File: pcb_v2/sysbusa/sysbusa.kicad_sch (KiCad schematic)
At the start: 62 parts, among them J1 bus ula 2, J10 bus rf16 3, J11 bus clu 2, J12 bus clu 3, J19 9V 1A, J2 bus ula 1, J20 VOLTMETER, J21 AMPMETER, J22 bus ioc 2, J23 bus ioc 1, J24 bus ioc 3, J26 bus clock, J3 bus rf16 1, J4 bus rf16 2, J5 bus mem 1, J6 bus mem 2, J7 bus clu 1, Q1 BC548, Q2 BC548, SW1 RESET, U1 MC14495P, U10 MC14495P, U11 ADDR N1, U12 DATA N0, U13 MC14495P, U14 RDADDR_LOW, U17 RDADDR_HIGH, U2 ADDR N3, U21 MC14495P, U22 WRADDR_HIGH, U23 WRADDR_LOW, U3 MC14495P, U31 MC14495P, U34 LM7805, U4 ADDR N2, U6 MC14495P, U7 DATA N1, U8 MC14495P, U9 ADDR N0

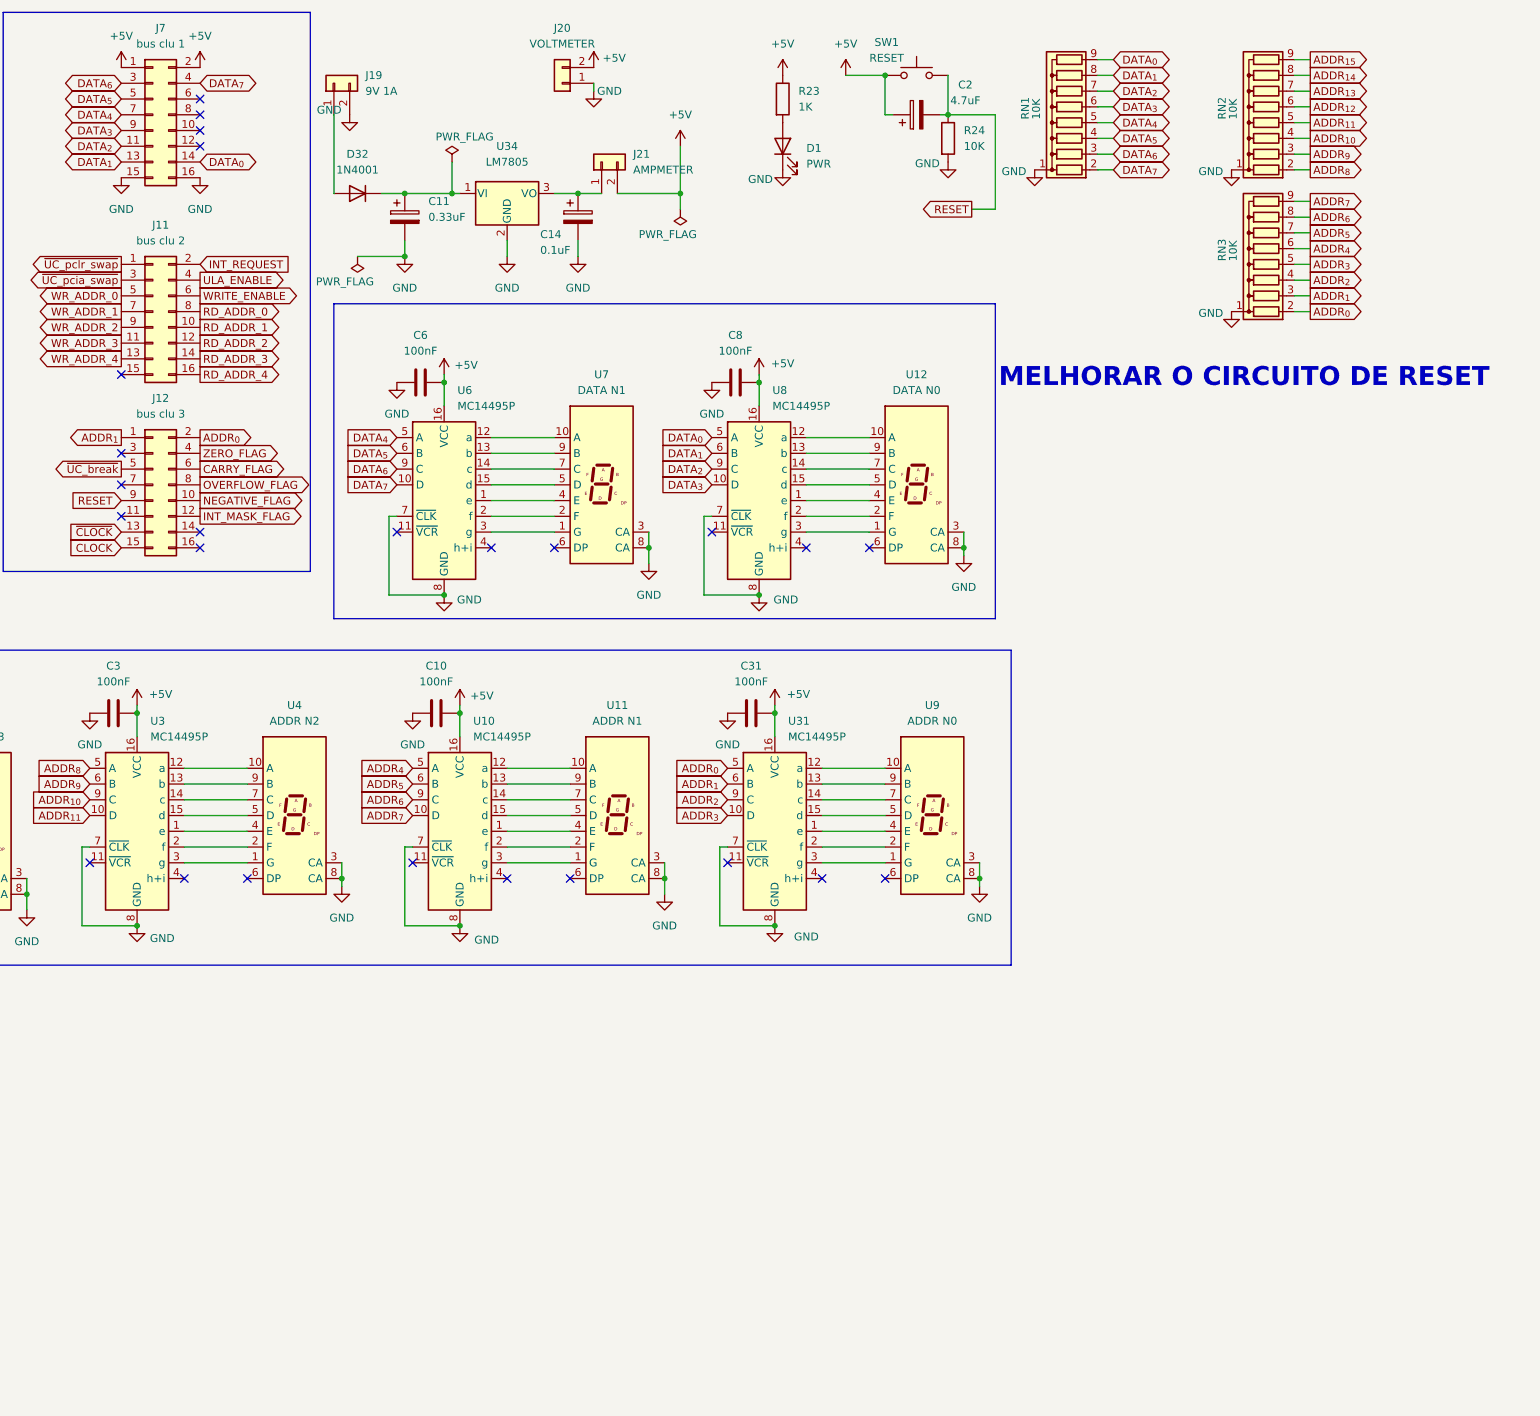
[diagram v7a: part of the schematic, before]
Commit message: melhoria no reset, para que seja acionado automaticamente ao ligar
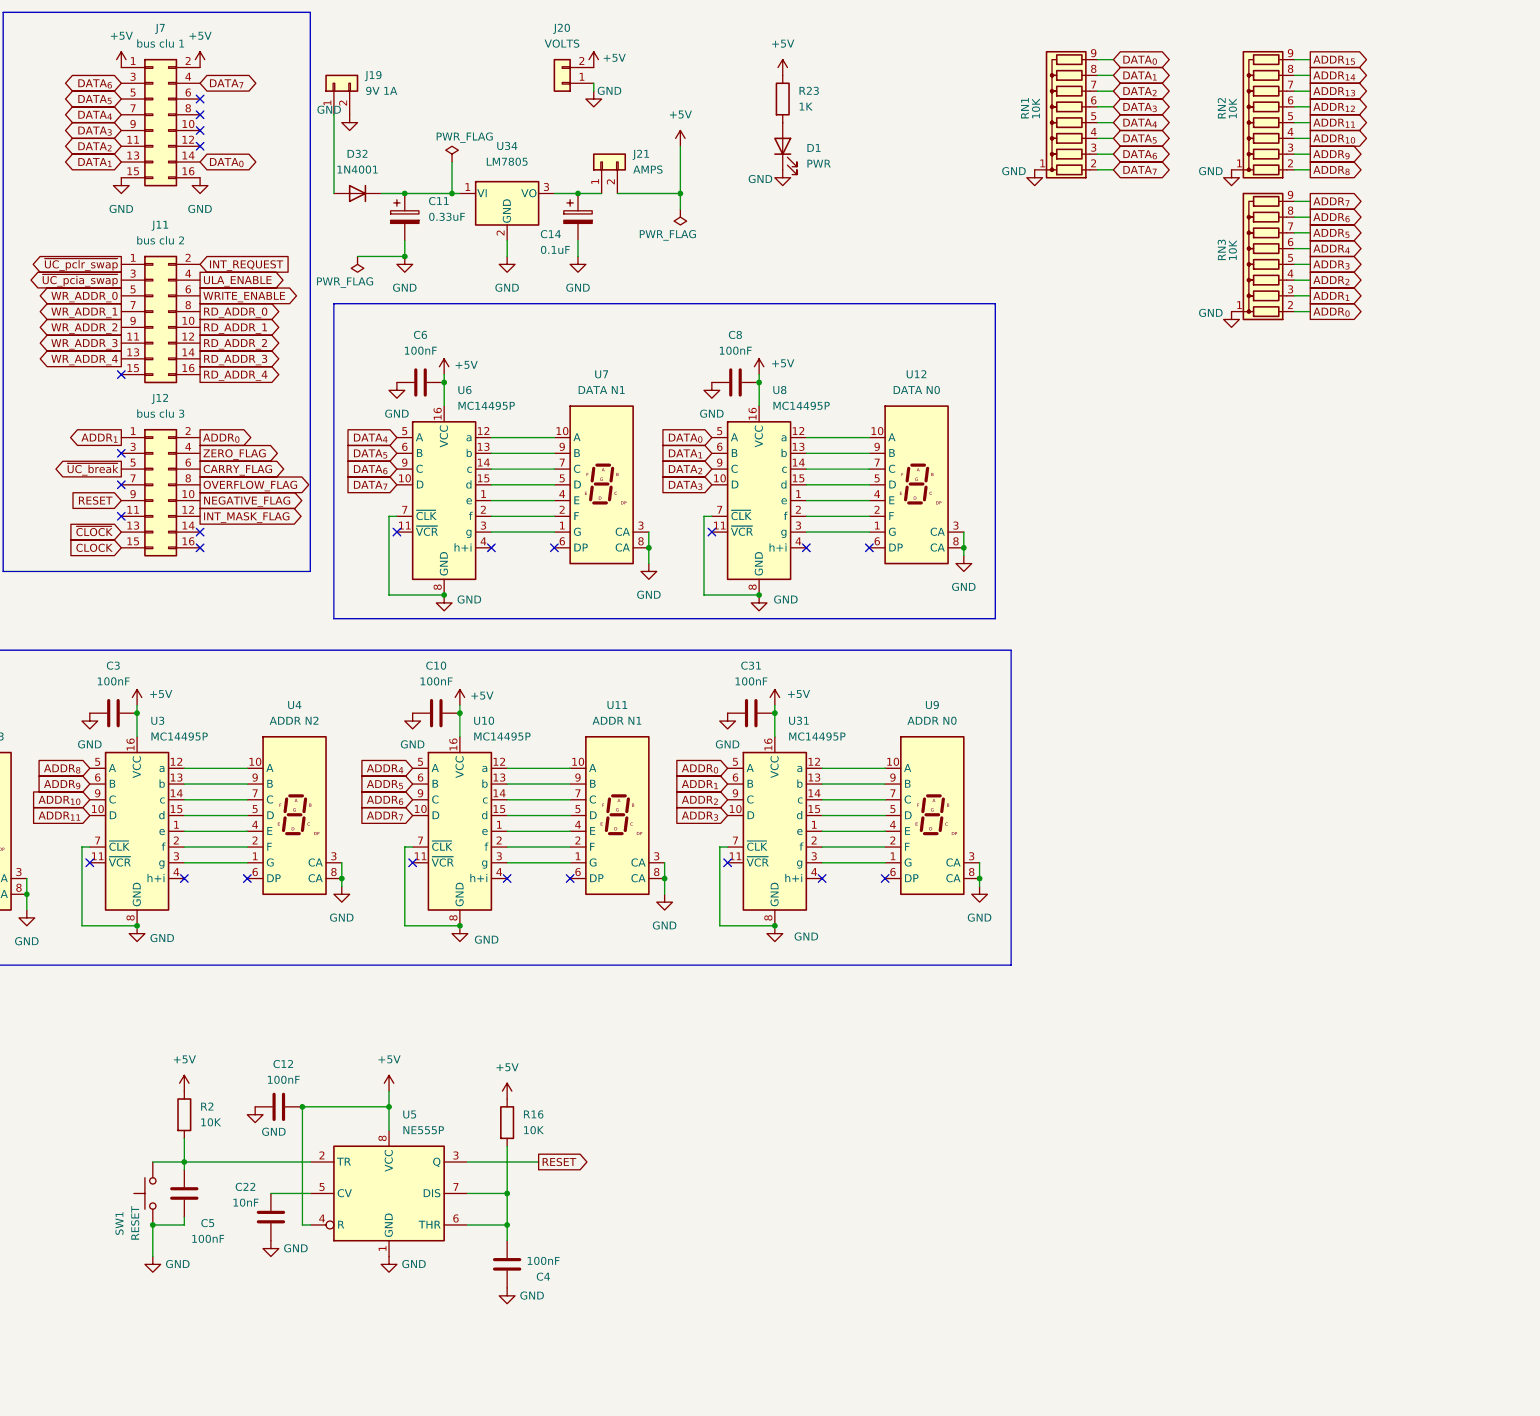
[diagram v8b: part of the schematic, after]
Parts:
- removed C2: 4.7uF, Capacitor_THT:CP_Radial_D5.0mm_P2.50mm, symbol Device:C_Polarized
- removed R24: 10K, Resistor_THT:R_Axial_DIN0207_L6.3mm_D2.5mm_P7.62mm_Horizontal, symbol Device:R
- added C12, C4, C5: 100nF, Capacitor_THT:C_Disc_D4.7mm_W2.5mm_P5.00mm, symbol Device:C
- added C22: 10nF, Capacitor_THT:C_Disc_D4.7mm_W2.5mm_P5.00mm, symbol Device:C
- added R16, R2: 10K, Resistor_THT:R_Axial_DIN0207_L6.3mm_D2.5mm_P7.62mm_Horizontal, symbol Device:R
- added U5: NE555P, Package_DIP:DIP-8_W7.62mm, symbol Timer:NE555P
- J20: value VOLTMETER -> VOLTS
- J21: value AMPMETER -> AMPS
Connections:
- net +5V: now also C12.2, R16.1, R2.1, U5.4 (R), U5.8 (VCC); no longer SW1.1
- net GND: now also SW1.1, C12.1, C22.1, C4.1, C5.1, U5.1 (GND)
- net RESET: now also U5.3 (Q); no longer SW1.2
- new net: C5.2, R2.2, SW1.2, U5.2 (TR)
- new net: C4.2, R16.2, U5.6 (THR), U5.7 (DIS)
- new net: C22.2, U5.5 (CV)
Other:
- note removed: "MELHORAR O CIRCUITO DE RESET"
- moved on the sheet: SW1
